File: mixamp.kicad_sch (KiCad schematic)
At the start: 21 parts, among them Q801 MMBT3904, T801 XFMR_RF_BIFILAR, U801 ADE-1

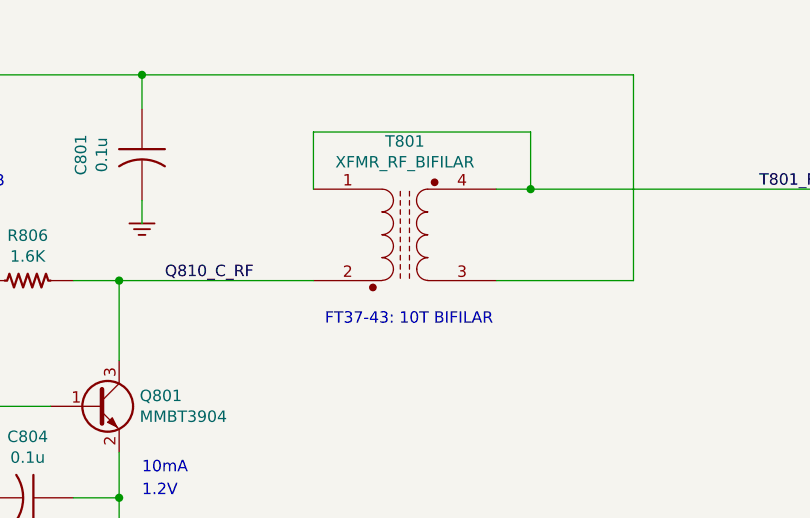
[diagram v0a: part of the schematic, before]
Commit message: Update pcb database to version 6
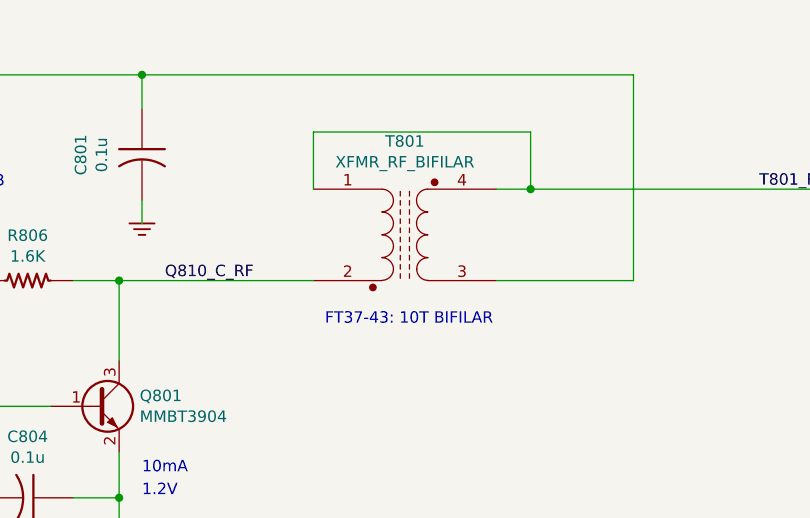
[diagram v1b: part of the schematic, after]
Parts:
- C801, C802, C803, C804, C805, C806: symbol Custom:C_US -> custom:C_US; PartNumber 800238-104 -> 800063-XXX
- Q801: symbol Custom:MMBT3904 -> custom:MMBT3904
- R801: symbol Custom:R_US -> custom:R_US; PartNumber 800235-100 -> 800XXX-XXX
- R802: symbol Custom:R_US -> custom:R_US; PartNumber 800235-180 -> 800XXX-XXX
- R803: symbol Custom:R_US -> custom:R_US; PartNumber 800235-822 -> 800XXX-XXX
- R804, R805: symbol Custom:R_US -> custom:R_US; PartNumber 800235-301 -> 800XXX-XXX
- R806: symbol Custom:R_US -> custom:R_US; PartNumber 800235-162 -> 800XXX-XXX
- R807: symbol Custom:R_US -> custom:R_US; PartNumber 800235-152 -> 800XXX-XXX
- R808: symbol Custom:R_US -> custom:R_US; PartNumber 800235-068 -> 800XXX-XXX
- R809: symbol Custom:R_US -> custom:R_US; PartNumber 800235-121 -> 800XXX-XXX
- R810: symbol Custom:R_US -> custom:R_US; PartNumber 800235-360 -> 800XXX-XXX
- R811, R812: symbol Custom:R_US -> custom:R_US; PartNumber 800235-151 -> 800XXX-XXX
- T801: symbol Custom:XFMR_RF_BIFILAR -> custom:XFMR_RF_BIFILAR
- U801: symbol Custom:ADE-1 -> custom:ADE-1

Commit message: Fix BOM part number errors and out of sync footprints which happened during conversion from Kicad 5 to 6
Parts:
- C801, C802, C803, C804, C805, C806: PartNumber 800063-XXX -> 800238-104
- R801: PartNumber 800XXX-XXX -> 800235-100
- R802: PartNumber 800XXX-XXX -> 800235-180
- R803: PartNumber 800XXX-XXX -> 800235-822
- R804, R805: PartNumber 800XXX-XXX -> 800235-301
- R806: PartNumber 800XXX-XXX -> 800235-162
- R807: PartNumber 800XXX-XXX -> 800235-152
- R808: PartNumber 800XXX-XXX -> 800235-068
- R809: PartNumber 800XXX-XXX -> 800235-121
- R810: PartNumber 800XXX-XXX -> 800235-360
- R811, R812: PartNumber 800XXX-XXX -> 800235-151
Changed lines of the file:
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@@
       (effects (font (size 1.524 1.524)))
     )
-    (property "PartNumber" "800XXX-XXX" (id 4) (at 149.86 51.562 90)
+    (property "PartNumber" "800235-162" (id 4) (at 149.86 51.562 90)
       (effects (font (size 1.524 1.524)) hide)
     )
@@
       (effects (font (size 1.524 1.524)))
     )
-    (property "PartNumber" "800063-XXX" (id 4) (at 140.97 46.99 0)
+    (property "PartNumber" "800238-104" (id 4) (at 140.97 46.99 0)
       (effects (font (size 1.524 1.524)) hide)
     )
@@
       (effects (font (size 1.524 1.524)))
     )
-    (property "PartNumber" "800XXX-XXX" (id 4) (at 162.052 76.2 90)
+    (property "PartNumber" "800235-121" (id 4) (at 162.052 76.2 90)
       (effects (font (size 1.524 1.524)) hide)
     )
@@
       (effects (font (size 1.524 1.524)))
     )
-    (property "PartNumber" "800063-XXX" (id 4) (at 161.29 71.12 0)
+    (property "PartNumber" "800238-104" (id 4) (at 161.29 71.12 0)
       (effects (font (size 1.524 1.524)) hide)
     )
@@
       (effects (font (size 1.524 1.524)))
     )
-    (property "PartNumber" "800XXX-XXX" (id 4) (at 140.462 76.2 90)
+    (property "PartNumber" "800235-068" (id 4) (at 140.462 76.2 90)
       (effects (font (size 1.524 1.524)) hide)
     )
@@
       (effects (font (size 1.524 1.524)))
     )
-    (property "PartNumber" "800063-XXX" (id 4) (at 115.57 54.61 0)
+    (property "PartNumber" "800238-104" (id 4) (at 115.57 54.61 0)
       (effects (font (size 1.524 1.524)) hide)
     )
@@
       (effects (font (size 1.524 1.524)))
     )
-    (property "PartNumber" "800XXX-XXX" (id 4) (at 120.142 76.2 90)
+    (property "PartNumber" "800235-152" (id 4) (at 120.142 76.2 90)
       (effects (font (size 1.524 1.524)) hide)
     )
@@
       (effects (font (size 1.524 1.524)))
     )
-    (property "PartNumber" "800XXX-XXX" (id 4) (at 120.142 31.75 90)
+    (property "PartNumber" "800235-822" (id 4) (at 120.142 31.75 90)
       (effects (font (size 1.524 1.524)) hide)
     )
@@
       (effects (font (size 1.524 1.524)))
     )
-    (property "PartNumber" "800063-XXX" (id 4) (at 160.02 19.05 0)
+    (property "PartNumber" "800238-104" (id 4) (at 160.02 19.05 0)
       (effects (font (size 1.524 1.524)) hide)
     )
@@
       (effects (font (size 1.524 1.524)))
     )
-    (property "PartNumber" "800XXX-XXX" (id 4) (at 99.06 28.702 90)
+    (property "PartNumber" "800235-100" (id 4) (at 99.06 28.702 90)
       (effects (font (size 1.524 1.524)) hide)
     )
@@
       (effects (font (size 1.524 1.524)))
     )
-    (property "PartNumber" "800XXX-XXX" (id 4) (at 59.182 39.37 90)
+    (property "PartNumber" "800235-301" (id 4) (at 59.182 39.37 90)
       (effects (font (size 1.524 1.524)) hide)
     )
@@
       (effects (font (size 1.524 1.524)))
     )
-    (property "PartNumber" "800XXX-XXX" (id 4) (at 43.942 39.37 90)
+    (property "PartNumber" "800235-301" (id 4) (at 43.942 39.37 90)
       (effects (font (size 1.524 1.524)) hide)
     )
@@
       (effects (font (size 1.524 1.524)))
     )
-    (property "PartNumber" "800XXX-XXX" (id 4) (at 49.53 38.862 90)
+    (property "PartNumber" "800235-180" (id 4) (at 49.53 38.862 90)
       (effects (font (size 1.524 1.524)) hide)
     )
@@
       (effects (font (size 1.524 1.524)))
     )
-    (property "PartNumber" "800063-XXX" (id 4) (at 100.33 132.08 0)
+    (property "PartNumber" "800238-104" (id 4) (at 100.33 132.08 0)
       (effects (font (size 1.524 1.524)) hide)
     )
@@
       (effects (font (size 1.524 1.524)))
     )
-    (property "PartNumber" "800063-XXX" (id 4) (at 157.48 132.08 0)
+    (property "PartNumber" "800238-104" (id 4) (at 157.48 132.08 0)
       (effects (font (size 1.524 1.524)) hide)
     )
@@
       (effects (font (size 1.524 1.524)))
     )
-    (property "PartNumber" "800XXX-XXX" (id 4) (at 108.712 138.43 90)
+    (property "PartNumber" "800235-151" (id 4) (at 108.712 138.43 90)
       (effects (font (size 1.524 1.524)) hide)
     )
@@
       (effects (font (size 1.524 1.524)))
     )
-    (property "PartNumber" "800XXX-XXX" (id 4) (at 127.762 138.43 90)
+    (property "PartNumber" "800235-151" (id 4) (at 127.762 138.43 90)
       (effects (font (size 1.524 1.524)) hide)
     )
@@
       (effects (font (size 1.524 1.524)))
     )
-    (property "PartNumber" "800XXX-XXX" (id 4) (at 115.57 136.652 90)
-      (effects (font (size 1.524 1.524)) hide)
-    )
+    (property "PartNumber" "800235-360" (id 4) (at 115.57 136.652 90)
+      (effects (font (size 1.524 1.524)) hide)
+    )

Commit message: trx_mobo_concept_2_B. Change design to use a dedicated 8V supply for the 2SC3357 parts. Add S-Meter connector. Change mic connector to 3 pins and add 8V sopower supply to pin 3.
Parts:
- C1601: renamed from C801; value 0.1u -> (none); footprint Capacitor_SMD:C_0805_2012Metric_Pad1.15x1.40mm_HandSolder -> (none)
- C1602: renamed from C802; value 0.1u -> (none); footprint Capacitor_SMD:C_0805_2012Metric_Pad1.15x1.40mm_HandSolder -> (none)
- C1603: renamed from C803; value 0.1u -> (none); footprint Capacitor_SMD:C_0805_2012Metric_Pad1.15x1.40mm_HandSolder -> (none)
- C1604: renamed from C804; value 0.1u -> (none); footprint Capacitor_SMD:C_0805_2012Metric_Pad1.15x1.40mm_HandSolder -> (none)
- C1605: renamed from C805; value 0.1u -> (none); footprint Capacitor_SMD:C_0805_2012Metric_Pad1.15x1.40mm_HandSolder -> (none)
- C1606: renamed from C806; value 0.1u -> (none); footprint Capacitor_SMD:C_0805_2012Metric_Pad1.15x1.40mm_HandSolder -> (none)
- Q1601: renamed from Q801; value MMBT3904 -> (none); footprint mods:SOT23-3-SAR -> (none)
- R1601: renamed from R801; value 10 -> (none); footprint Resistor_SMD:R_0805_2012Metric_Pad1.15x1.40mm_HandSolder -> (none)
- R1602: renamed from R802; value 18 -> (none); footprint Resistor_SMD:R_0805_2012Metric_Pad1.15x1.40mm_HandSolder -> (none)
- R1603: renamed from R803; value 8.2K -> (none); footprint Resistor_SMD:R_0805_2012Metric_Pad1.15x1.40mm_HandSolder -> (none)
- R1604: renamed from R804; value 300 -> (none); footprint Resistor_SMD:R_0805_2012Metric_Pad1.15x1.40mm_HandSolder -> (none)
- R1605: renamed from R805; value 300 -> (none); footprint Resistor_SMD:R_0805_2012Metric_Pad1.15x1.40mm_HandSolder -> (none)
- R1606: renamed from R806; value 1.6K -> (none); footprint Resistor_SMD:R_0805_2012Metric_Pad1.15x1.40mm_HandSolder -> (none)
- R1607: renamed from R807; value 1.5K -> (none); footprint Resistor_SMD:R_0805_2012Metric_Pad1.15x1.40mm_HandSolder -> (none)
- R1608: renamed from R808; value 6.8 -> (none); footprint Resistor_SMD:R_0805_2012Metric_Pad1.15x1.40mm_HandSolder -> (none)
- R1609: renamed from R809; value 120 -> (none); footprint Resistor_SMD:R_0805_2012Metric_Pad1.15x1.40mm_HandSolder -> (none)
- R1610: renamed from R810; value 36 -> (none); footprint Resistor_SMD:R_0805_2012Metric_Pad1.15x1.40mm_HandSolder -> (none)
- R1611: renamed from R811; value 150 -> (none); footprint Resistor_SMD:R_0805_2012Metric_Pad1.15x1.40mm_HandSolder -> (none)
- R1612: renamed from R812; value 150 -> (none); footprint Resistor_SMD:R_0805_2012Metric_Pad1.15x1.40mm_HandSolder -> (none)
- T1601: renamed from T801; value XFMR_RF_BIFILAR -> (none); footprint mods:XFMR_Handwound_FT37 -> (none)
- U1601: renamed from U801; value ADE-1 -> (none); footprint mods:MCL-6-SMD_7R97X5R59 -> (none)
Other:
- note added: "FT37-43: 10T #30 AWG BIFILAR"
- note removed: "FT37-43: 10T BIFILAR"
